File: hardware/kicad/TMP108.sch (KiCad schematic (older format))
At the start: 33 parts, among them J1 Screw_Terminal_01x08, J2 Screw_Terminal_01x08, J3 CAN, SW1 PRG, SW2 BUS, SW3 PRG-VALUE, U1 Teensy_3.2, U2 TMR-1211, U3 MCP2551-I-P

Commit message: Tweak
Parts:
- removed C1: 1000uF, Capacitor_THT:CP_Radial_D8.0mm_P5.00mm, symbol Device:CP
- removed C2: 100nF, Capacitor_THT:C_Rect_L4.6mm_W3.0mm_P2.50mm_MKS02_FKP02, symbol Device:C
- removed C3: 100n, Capacitor_THT:C_Rect_L4.6mm_W3.0mm_P2.50mm_MKS02_FKP02, symbol Device:C
- removed D1: INST, LED_THT:LED_D1.8mm_W3.3mm_H2.4mm, symbol Device:LED
- removed D2: SRCE, LED_THT:LED_D1.8mm_W3.3mm_H2.4mm, symbol Device:LED
- removed D3: SETP, LED_THT:LED_D1.8mm_W3.3mm_H2.4mm, symbol Device:LED
- removed D4: TINT, LED_THT:LED_D1.8mm_W3.3mm_H2.4mm, symbol Device:LED
- removed D5: PWR, LED_THT:LED_D3.0mm_FlatTop, symbol Device:LED
- removed F1: 1A, Fuse:Fuse_Littelfuse_395Series, symbol Device:Polyfuse
- removed J1, J2: Screw_Terminal_01x08, PDJR-connectors:Phoenix-FK-MPT-8-3,5, symbol Connector:Screw_Terminal_01x08
- removed J3: CAN, TerminalBlock_Phoenix:TerminalBlock_Phoenix_MPT-0,5-5-2.54_1x05_P2.54mm_Horizontal, symbol Connector:Screw_Terminal_01x05
- removed R1, R10, R11, R12, R13: 380R, Resistor_THT:R_Axial_DIN0207_L6.3mm_D2.5mm_P7.62mm_Horizontal, symbol Device:R
- removed R14: 120R, Resistor_THT:R_Axial_DIN0207_L6.3mm_D2.5mm_P7.62mm_Horizontal, symbol Device:R
- removed R15: 4K7, Resistor_THT:R_Axial_DIN0207_L6.3mm_D2.5mm_P7.62mm_Horizontal, symbol Device:R
- removed R2, R3, R4, R5, R6, R7, R8, R9: 2K2, Resistor_THT:R_Axial_DIN0207_L6.3mm_D2.5mm_P7.62mm_Horizontal, symbol Device:R
- removed SW1: PRG, Button_Switch_THT:SW_PUSH_6mm_H4.3mm, symbol Switch:SW_Push
- removed SW2: BUS, Package_DIP:DIP-4_W7.62mm_LongPads, symbol Switch:SW_DIP_x02
- removed SW3: PRG-VALUE, Package_DIP:DIP-16_W7.62mm, symbol Switch:SW_DIP_x08
- removed U1: Teensy_3.2, Package_DIP:DIP-28_W15.24mm_LongPads, symbol pdjr:Teensy_3.2
- removed U2: TMR-1211, PDJR-connectors:TMR-1-1211, symbol pdjr:TMR-1211
- removed U3: MCP2551-I-P, Package_DIP:DIP-8_W7.62mm, symbol Interface_CAN_LIN:MCP2551-I-P
- added C?: 1nF, symbol Device:C_Small
- added C?: 20nF, symbol Device:C_Small
- added C?: 10uF, symbol Device:C_Small
- added D? (x4): D_Schottky_Small, symbol Device:D_Schottky_Small
- added Q? (x2): 2N3904, Package_TO_SOT_THT:TO-92_Inline, symbol Transistor_BJT:2N3904
- added R?: 2K2, Resistor_THT:R_Axial_DIN0207_L6.3mm_D2.5mm_P7.62mm_Horizontal, symbol Device:R
- added R?: 390R, Resistor_THT:R_Axial_DIN0207_L6.3mm_D2.5mm_P7.62mm_Horizontal, symbol Device:R
- added R?: 75R, Resistor_THT:R_Axial_DIN0207_L6.3mm_D2.5mm_P7.62mm_Horizontal, symbol Device:R
- added R?: 10K, Resistor_THT:R_Axial_DIN0207_L6.3mm_D2.5mm_P7.62mm_Horizontal, symbol Device:R
- added R?: 1K, Resistor_THT:R_Axial_DIN0207_L6.3mm_D2.5mm_P7.62mm_Horizontal, symbol Device:R
- added T?: Transformer_SP_1S, symbol Device:Transformer_SP_1S
- added TP? (x8): TestPoint_Small, symbol Connector:TestPoint_Small
- added U?: MAX845, symbol pdjr:MAX845
- added U?: MAX6576, symbol pdjr:MAX6576
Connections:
- net labels added: D19, D20, D21, D23
- net labels removed: ADDR_0, ADDR_1, ADDR_2, ADDR_3, ADDR_4, ADDR_5, ADDR_6, ADDR_7, CAN_H, CAN_L, CAN_RX, CAN_SCR, CAN_TX, LED_INSTANCE, LED_INTERVAL, LED_PWR, LED_SETPOINT, LED_SOURCE, NET_C, NET_S, SENSOR_T0, SENSOR_T1, SENSOR_T2, SENSOR_T3, SENSOR_T4, SENSOR_T5, SENSOR_T6, SENSOR_T7, TERM_A, TERM_B
- wire segments 131 -> 76
- no-connect marks 6 -> 0
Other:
- note removed: "12/5 V DC-DC CONVERTER"
- note removed: "CAN INTERFACE"

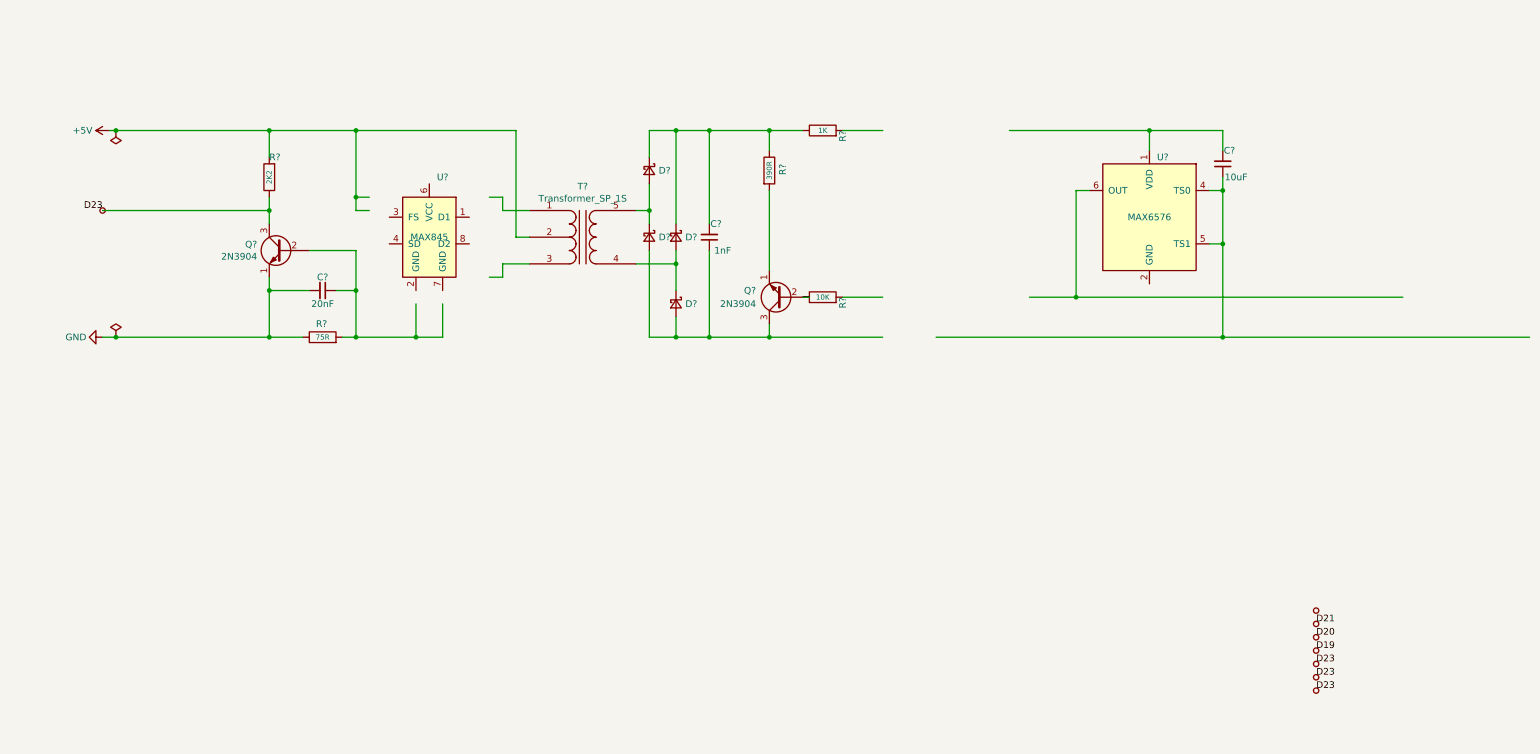
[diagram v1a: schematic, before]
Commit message: Isolate temperature sensors
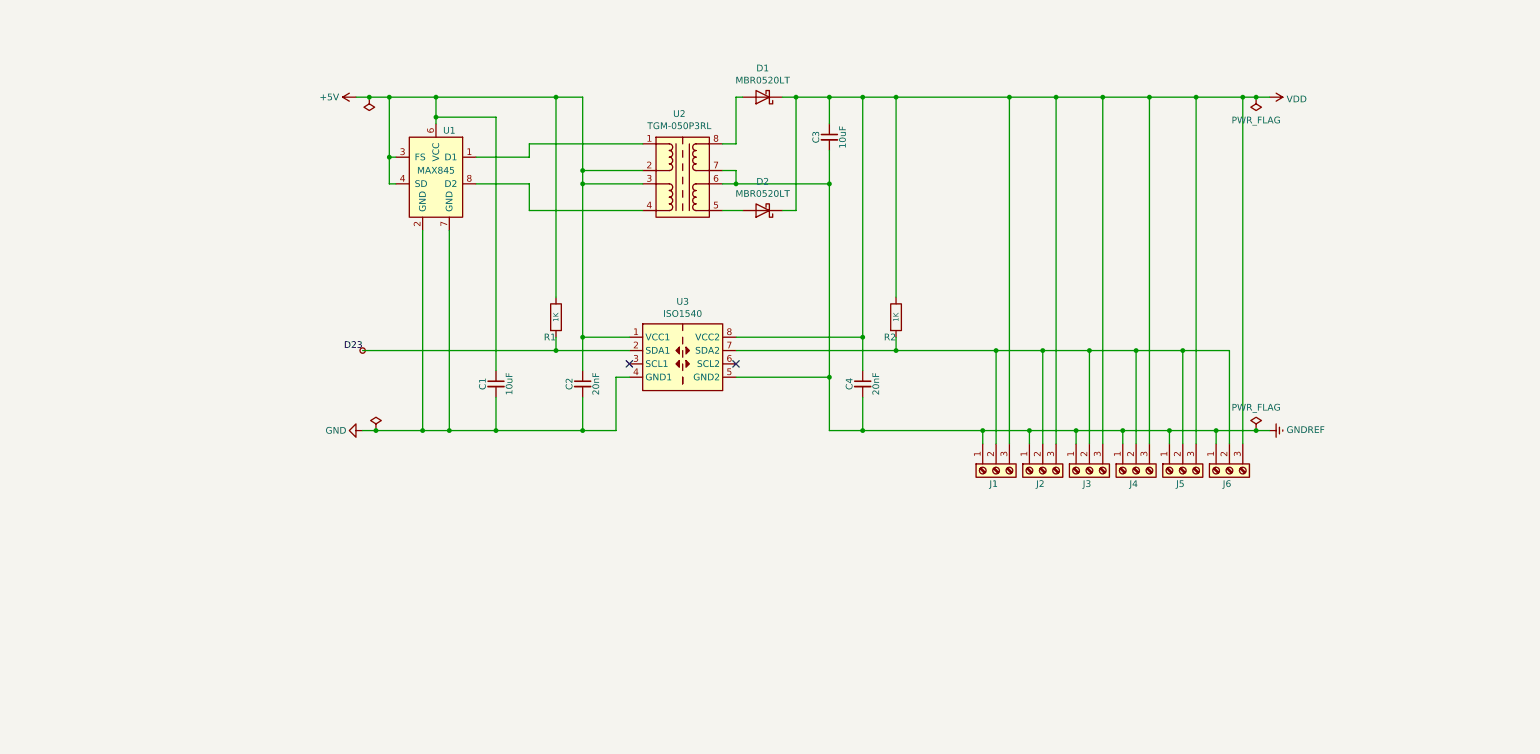
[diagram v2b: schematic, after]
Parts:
- removed C?: 1nF, symbol Device:C_Small
- removed C?: 20nF, symbol Device:C_Small
- removed C?: 10uF, symbol Device:C_Small
- removed D? (x4): D_Schottky_Small, symbol Device:D_Schottky_Small
- removed Q? (x2): 2N3904, Package_TO_SOT_THT:TO-92_Inline, symbol Transistor_BJT:2N3904
- removed R?: 2K2, Resistor_THT:R_Axial_DIN0207_L6.3mm_D2.5mm_P7.62mm_Horizontal, symbol Device:R
- removed R?: 390R, Resistor_THT:R_Axial_DIN0207_L6.3mm_D2.5mm_P7.62mm_Horizontal, symbol Device:R
- removed R?: 75R, Resistor_THT:R_Axial_DIN0207_L6.3mm_D2.5mm_P7.62mm_Horizontal, symbol Device:R
- removed R?: 10K, Resistor_THT:R_Axial_DIN0207_L6.3mm_D2.5mm_P7.62mm_Horizontal, symbol Device:R
- removed R?: 1K, Resistor_THT:R_Axial_DIN0207_L6.3mm_D2.5mm_P7.62mm_Horizontal, symbol Device:R
- removed T?: Transformer_SP_1S, symbol Device:Transformer_SP_1S
- removed TP? (x8): TestPoint_Small, symbol Connector:TestPoint_Small
- removed U?: MAX6576, symbol pdjr:MAX6576
- added C1, C3: 10uF, Capacitor_SMD:C_0805_2012Metric, symbol Device:C_Small
- added C2, C4: 20nF, Capacitor_SMD:C_0805_2012Metric, symbol Device:C_Small
- added D1, D2: MBR0520LT, Diode_SMD:D_SOD-123, symbol Diode:MBR0520LT
- added J1, J2, J3, J4, J5, J6: Screw_Terminal_01x03, Connector_PinHeader_2.54mm:PinHeader_1x03_P2.54mm_Vertical, symbol Connector:Screw_Terminal_01x03
- added R1, R2: 1K, Resistor_SMD:R_0805_2012Metric, symbol Device:R
- added U2: TGM-050P3RL, PDJR-transformers:TGM-010P3RL, symbol pdjr:TGM-050P3RL
- added U3: ISO1540, Package_SO:SOIC-8_3.9x4.9mm_P1.27mm, symbol Isolator:ISO1540
- U1: renamed from U?; footprint (none) -> Package_SO:TSSOP-8_3x3mm_P0.65mm
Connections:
- net labels added: GNDREF, TestPoint_Small, VDD
- net labels removed: D19, D20, D21
- wire segments 76 -> 109
- no-connect marks 0 -> 2
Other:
- moved on the sheet: U1

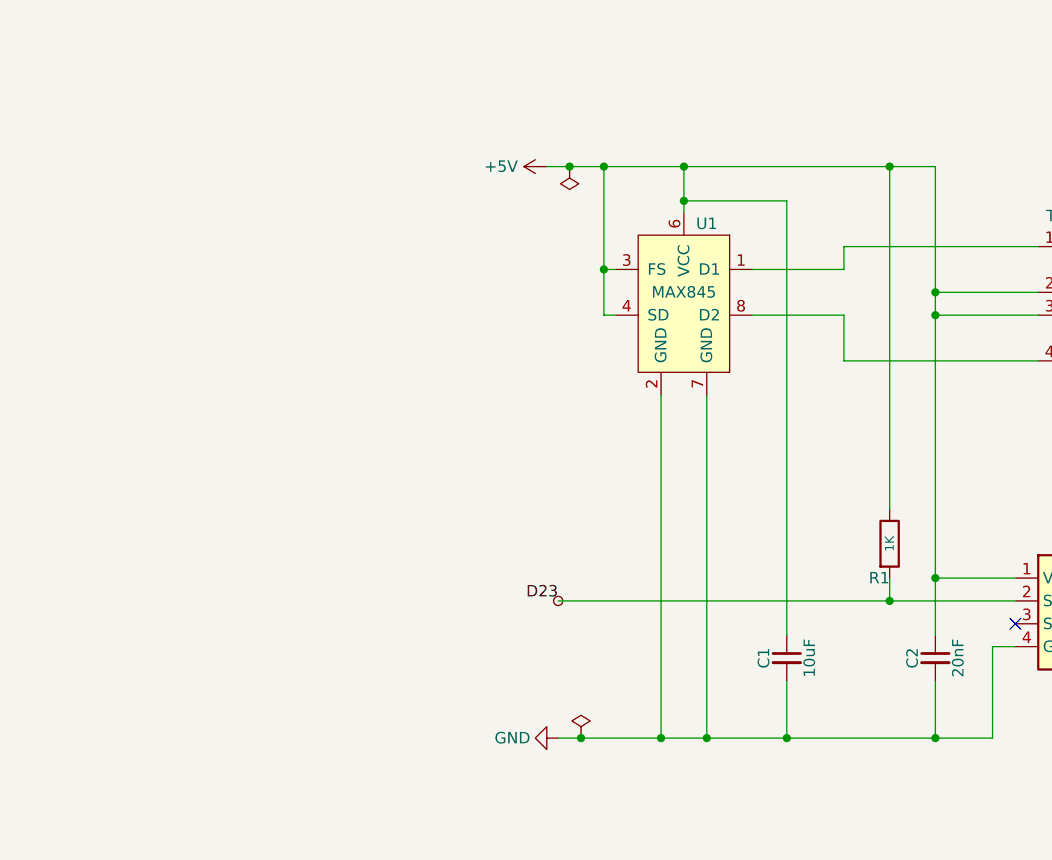
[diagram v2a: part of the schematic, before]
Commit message: Voltage shift D23
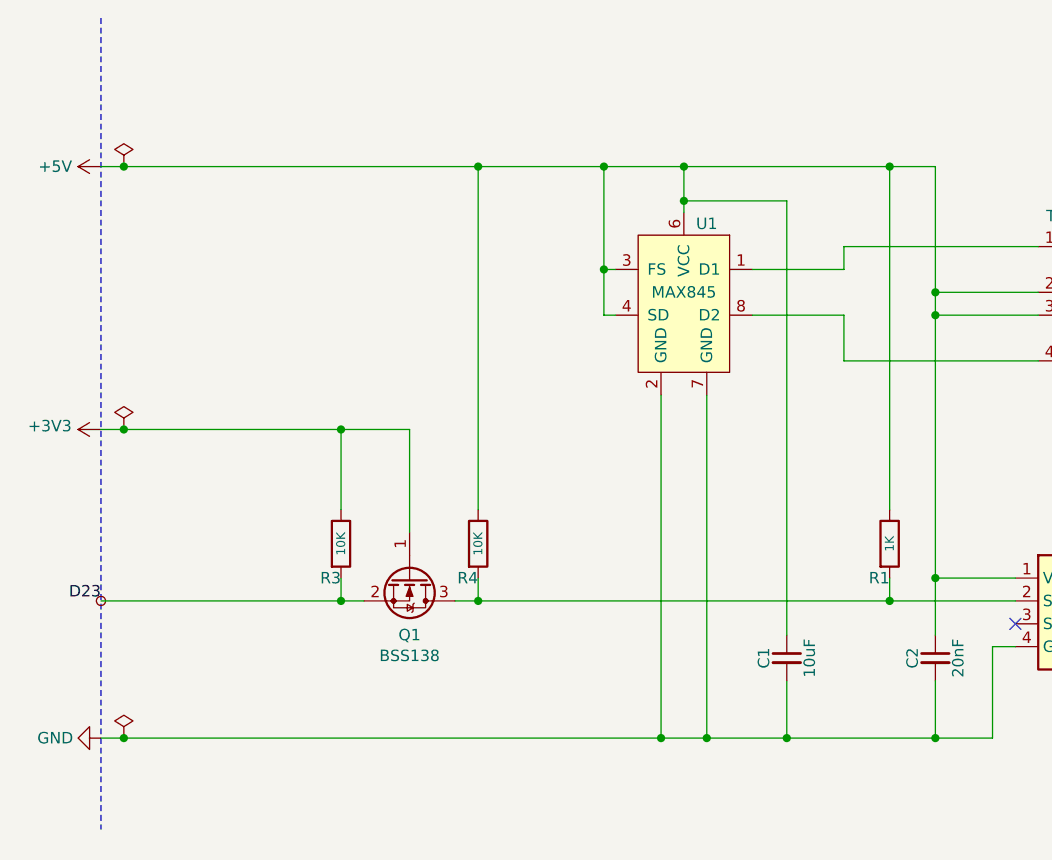
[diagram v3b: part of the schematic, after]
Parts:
- added Q1: BSS138, Package_TO_SOT_SMD:SOT-23, symbol Transistor_FET:BSS138
- added R3, R4: 10K, Resistor_SMD:R_0805_2012Metric, symbol Device:R
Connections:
- net +5V: now also R4.1
- net D23: now also Q1.2 (S), R3.2; no longer R1.2, U3.2 (SDA1)
- new net: Q1.3 (D), R1.2, R4.2, U3.2 (SDA1)
- new net +3V3: Q1.1 (G), R3.1
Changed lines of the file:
@@
 L power:GND #PWR02
 U 1 1 6109972B
-P 3000 3650
-F 0 "#PWR02" H 3000 3400 50  0001 C CNN
-F 1 "GND" V 3000 3450 50  0000 C CNN
-F 2 "" H 3000 3650 50  0001 C CNN
-F 3 "" H 3000 3650 50  0001 C CNN
-	1    3000 3650
+P 1000 3650
+F 0 "#PWR02" H 1000 3400 50  0001 C CNN
+F 1 "GND" V 1000 3450 50  0000 C CNN
+F 2 "" H 1000 3650 50  0001 C CNN
+F 3 "" H 1000 3650 50  0001 C CNN
+	1    1000 3650
 	0    1    1    0
 $EndComp
@@
 L power:+5V #PWR01
 U 1 1 606B2F50
-P 2950 1150
-F 0 "#PWR01" H 2950 1000 50  0001 C CNN
-F 1 "+5V" V 2950 1350 50  0000 C CNN
-F 2 "" H 2950 1150 50  0001 C CNN
-F 3 "" H 2950 1150 50  0001 C CNN
-	1    2950 1150
+P 1000 1150
+F 0 "#PWR01" H 1000 1000 50  0001 C CNN
+F 1 "+5V" V 1000 1350 50  0000 C CNN
+F 2 "" H 1000 1150 50  0001 C CNN
+F 3 "" H 1000 1150 50  0001 C CNN
+	1    1000 1150
 	0    -1   -1   0
 $EndComp
@@
 L Connector:TestPoint_Small #TP1
 U 1 1 63AC2648
-P 3000 3050
-F 0 "#TP1" H 3048 3096 50  0001 L CNN
-F 1 "TestPoint_Small" H 3048 3050 50  0001 L CNN
-F 2 "" H 3200 3050 50  0001 C CNN
-F 3 "~" H 3200 3050 50  0001 C CNN
-	1    3000 3050
+P 1000 3050
+F 0 "#TP1" H 1048 3096 50  0001 L CNN
+F 1 "TestPoint_Small" H 1048 3050 50  0001 L CNN
+F 2 "" H 1200 3050 50  0001 C CNN
+F 3 "~" H 1200 3050 50  0001 C CNN
+	1    1000 3050
 	-1   0    0    1
 $EndComp
 Wire Wire Line
-	2950 1150 3050 1150
+	1000 1150 1100 1150
 $Comp
 L power:PWR_FLAG #FLG01
 U 1 1 63ADE24D
-P 3050 1150
-F 0 "#FLG01" H 3050 1225 50  0001 C CNN
-F 1 "PWR_FLAG" H 3050 1323 50  0001 C CNN
-F 2 "" H 3050 1150 50  0001 C CNN
-F 3 "~" H 3050 1150 50  0001 C CNN
-	1    3050 1150
-	-1   0    0    1
+P 1100 1150
+F 0 "#FLG01" H 1100 1225 50  0001 C CNN
+F 1 "PWR_FLAG" H 1100 1323 50  0001 C CNN
+F 2 "" H 1100 1150 50  0001 C CNN
+F 3 "~" H 1100 1150 50  0001 C CNN
+	1    1100 1150
+	1    0    0    -1
 $EndComp
 $Comp
 L power:PWR_FLAG #FLG02
 U 1 1 63ADECFA
-P 3100 3650
-F 0 "#FLG02" H 3100 3725 50  0001 C CNN
-F 1 "PWR_FLAG" H 3100 3823 50  0001 C CNN
-F 2 "" H 3100 3650 50  0001 C CNN
-F 3 "~" H 3100 3650 50  0001 C CNN
-	1    3100 3650
+P 1100 3650
+F 0 "#FLG02" H 1100 3725 50  0001 C CNN
+F 1 "PWR_FLAG" H 1100 3823 50  0001 C CNN
+F 2 "" H 1100 3650 50  0001 C CNN
+F 3 "~" H 1100 3650 50  0001 C CNN
+	1    1100 3650
 	1    0    0    -1
 $EndComp
@@
 	0    -1   1    0
 $EndComp
-Text Label 3000 3050 2    50   ~ 0
+Text Label 1000 3050 2    50   ~ 0
 D23
 $Comp
@@
 	4450 2950 4450 3050
 Wire Wire Line
-	4450 3050 3000 3050
+	4450 3050 2650 3050
 Wire Wire Line
 	4450 2650 4450 1150
@@
 	3450 2150 3450 3650
 Wire Wire Line
-	3000 3650 3100 3650
+	1000 3650 1100 3650
 Connection ~ 3450 3650
-Connection ~ 3100 3650
-Wire Wire Line
-	3100 3650 3450 3650
-Wire Wire Line
-	3050 1150 3200 1150
-Connection ~ 3050 1150
-Connection ~ 3200 1150
+Connection ~ 1100 3650
+Wire Wire Line
+	1100 3650 3450 3650
 $Comp
 L Device:C_Small C1
@@
 	9800 1150 9700 1150
 Connection ~ 9700 1150
+$Comp
+L Transistor_FET:BSS138 Q1
+U 1 1 63B7376E
+P 2350 2950
+F 0 "Q1" V 2599 2950 50  0000 C CNN
+F 1 "BSS138" V 2690 2950 50  0000 C CNN
+F 2 "Package_TO_SOT_SMD:SOT-23" H 2550 2875 50  0001 L CIN
+F 3 "https://www.onsemi.com/pub/Collateral/BSS138-D.PDF" H 2350 2950 50  0001 L CNN
+	1    2350 2950
+	0    1    1    0
+$EndComp
+$Comp
+L Device:R R3
+U 1 1 63B7D130
+P 2050 2800
+F 0 "R3" H 2050 2650 50  0000 R CNN
+F 1 "10K" V 2050 2800 39  0000 C CNN
+F 2 "Resistor_SMD:R_0805_2012Metric" V 1980 2800 50  0001 C CNN
+F 3 "~" H 2050 2800 50  0001 C CNN
+	1    2050 2800
+	1    0    0    -1
+$EndComp
+$Comp
+L Device:R R4
+U 1 1 63B7D42E
+P 2650 2800
+F 0 "R4" H 2650 2650 50  0000 R CNN
+F 1 "10K" V 2650 2800 39  0000 C CNN
+F 2 "Resistor_SMD:R_0805_2012Metric" V 2580 2800 50  0001 C CNN
+F 3 "~" H 2650 2800 50  0001 C CNN
+	1    2650 2800
+	1    0    0    -1
+$EndComp
+$Comp
+L power:+3V3 #PWR03
+U 1 1 63B7DC97
+P 1000 2300
+F 0 "#PWR03" H 1000 2150 50  0001 C CNN
+F 1 "+3V3" V 1015 2428 50  0000 L CNN
+F 2 "" H 1000 2300 50  0001 C CNN
+F 3 "" H 1000 2300 50  0001 C CNN
+	1    1000 2300
+	0    -1   -1   0
+$EndComp
+Wire Notes Line
+	1000 500  1000 4050
+Wire Wire Line
+	2650 2950 2650 3050
+Connection ~ 2650 3050
+Wire Wire Line
+	2650 3050 2550 3050
+Wire Wire Line
+	2150 3050 2050 3050
+Wire Wire Line
+	2050 3050 2050 2950
+Wire Wire Line
+	1000 2300 1100 2300
+Wire Wire Line
+	2050 2300 2350 2300
+Connection ~ 2050 2300
+Wire Wire Line
+	2050 2300 2050 2650
+Wire Wire Line
+	2350 2300 2350 2750
+Wire Wire Line
+	2650 2650 2650 1150
+Wire Wire Line
+	1000 3050 2050 3050
+Connection ~ 2050 3050
+Connection ~ 1100 1150
+Wire Wire Line
+	1100 1150 2650 1150
+Wire Wire Line
+	2650 1150 3200 1150
+Connection ~ 2650 1150
+Connection ~ 3200 1150
+$Comp
+L power:PWR_FLAG #FLG0103
+U 1 1 63C171FE
+P 1100 2300
+F 0 "#FLG0103" H 1100 2375 50  0001 C CNN
+F 1 "PWR_FLAG" H 1100 2473 50  0001 C CNN
+F 2 "" H 1100 2300 50  0001 C CNN
+F 3 "~" H 1100 2300 50  0001 C CNN
+	1    1100 2300
+	1    0    0    -1
+$EndComp
+Connection ~ 1100 2300
+Wire Wire Line
+	1100 2300 2050 2300
 $EndSCHEMATC
